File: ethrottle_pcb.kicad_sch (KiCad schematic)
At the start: 61 parts, among them J1 ATM15-08PA-BM02, Q1 ZXTR2105F-7, Q2 DDTC124XCA-7-F, U1 MCP6004, U2 MCP6004, U3 MCP6004, U4 UB2-5NUN

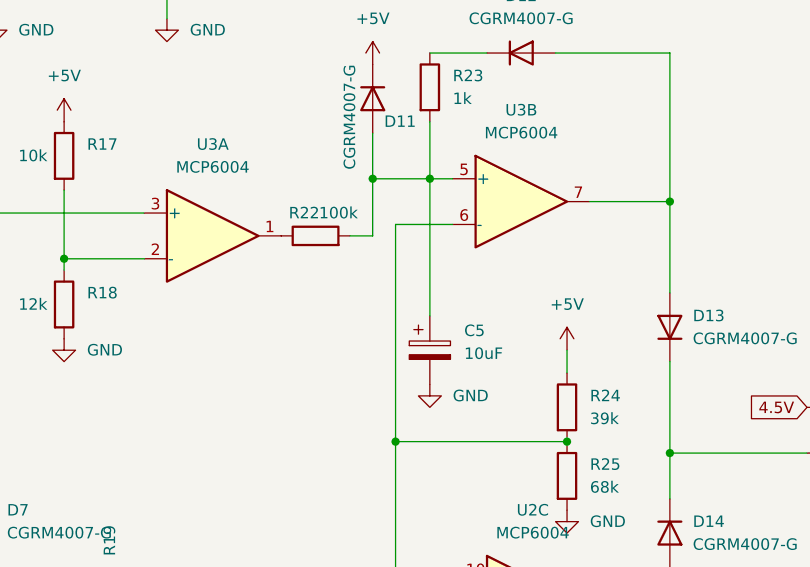
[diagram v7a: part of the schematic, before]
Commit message: changed latching RC circuit to 10k and 100uF, basically the leakage current of d11 might self trip the circuit after some time
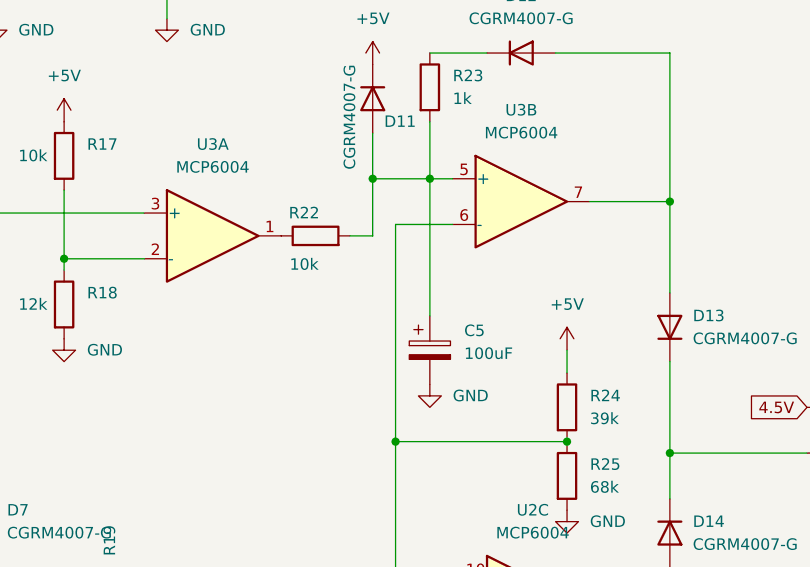
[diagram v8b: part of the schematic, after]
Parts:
- C5: value 10uF -> 100uF
- R22: value 100k -> 10k
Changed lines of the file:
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@@
     (in_bom yes) (on_board yes)
     (property "Reference" "R22" (id 0) (at 149.86 59.69 90))
-    (property "Value" "100k" (id 1) (at 153.67 59.69 90))
+    (property "Value" "10k" (id 1) (at 149.86 65.405 90))
     (property "Footprint" "Resistor_SMD:R_01005_0402Metric" (id 2) (at 151.13 64.008 90)
       (effects (font (size 1.27 1.27)) hide)
@@
       (effects (font (size 1.27 1.27)) (justify left))
     )
-    (property "Value" "10uF" (id 1) (at 167.64 75.3109 0)
+    (property "Value" "100uF" (id 1) (at 167.64 75.3109 0)
       (effects (font (size 1.27 1.27)) (justify left))
     )
@@
     )
     (path "/37979d87-fb1f-4526-ab76-2f015850d816"
-      (reference "C5") (unit 1) (value "10uF") (footprint "Capacitor_SMD:C_0805_2012Metric")
+      (reference "C5") (unit 1) (value "100uF") (footprint "Capacitor_SMD:C_0805_2012Metric")
     )
     (path "/bd515c98-1462-4b1d-bef4-56a57db1aee7"
@@
     )
     (path "/32cc6bc3-7e6d-44a9-b6c8-2ea259f6f98a"
-      (reference "R22") (unit 1) (value "100k") (footprint "Resistor_SMD:R_01005_0402Metric")
+      (reference "R22") (unit 1) (value "10k") (footprint "Resistor_SMD:R_01005_0402Metric")
     )
     (path "/b1278799-ce6a-44fc-89c8-99cd1c12e9c4"
